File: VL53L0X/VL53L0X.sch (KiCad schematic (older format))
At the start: 23 parts, among them J1 Conn_01x06, J2 Conn_01x04, J3 Conn_01x06, J4 Conn_01x04, Q1 BSS138DW, Q2 BSS138DW, U1 AP2127K-2.8, U2 VL53L0X

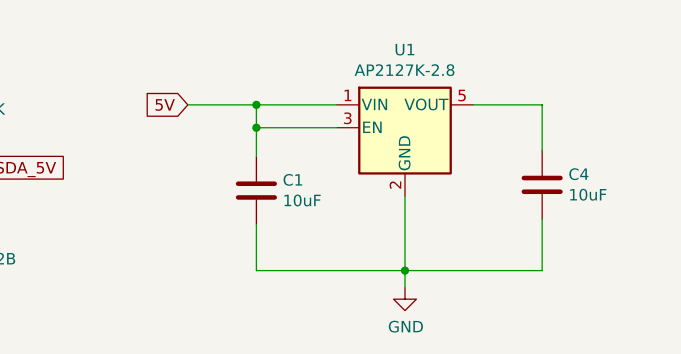
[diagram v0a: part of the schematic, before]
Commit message: Schematic and 3D render updates
Multiple boards
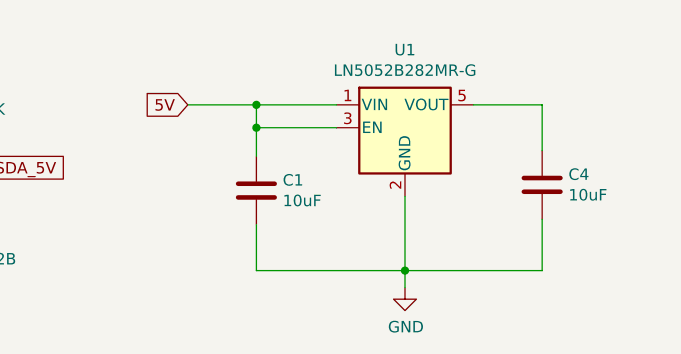
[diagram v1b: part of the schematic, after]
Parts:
- U1: value AP2127K-2.8 -> LN5052B282MR-G
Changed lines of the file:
@@
 P 5900 1050
 F 0 "U1" H 5900 1390 50  0000 C CNN
-F 1 "AP2127K-2.8" H 5900 1300 50  0000 C CNN
+F 1 "LN5052B282MR-G" H 5900 1300 50  0000 C CNN
 F 2 "Package_TO_SOT_SMD:SOT-23-5" H 5900 1375 50  0001 C CNN
 F 3 "https://datasheet.lcsc.com/szlcsc/NATLINEAR-LN5052B282MR-G_C185101.pdf" H 5900 1150 50  0001 C CNN
